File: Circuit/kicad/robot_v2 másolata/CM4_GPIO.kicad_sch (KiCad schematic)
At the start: 28 parts, among them J1 Conn_01x03, J2 Conn_02x07_Odd_Even, J3 Conn_01x03, J7 Micro_SD_Card_Det, J8 THD-20-R, J9 THD-02-R, U1 TPD4EUSB30, U18 RT9742GGJ5, U2 TPD4EUSB30, U3 MagJack-A70-112-331N126, U5 74LVC1G07SE-7, U9 74LVC1G07SE-7

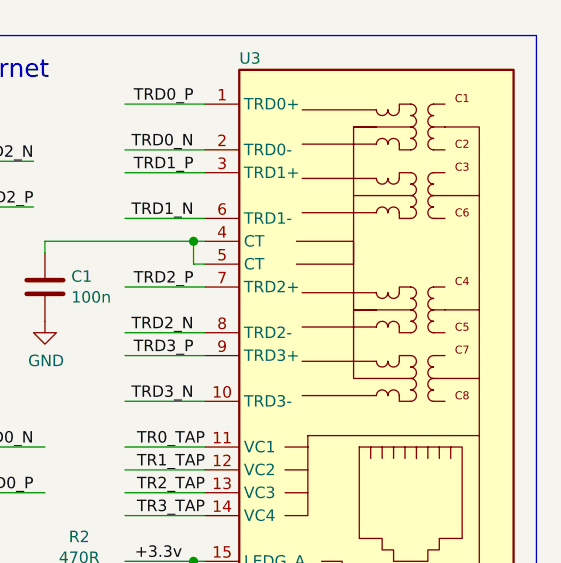
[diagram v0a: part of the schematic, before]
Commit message: kicad i2c schematic updated: gyto i2c bugfixes, +add new datasheets
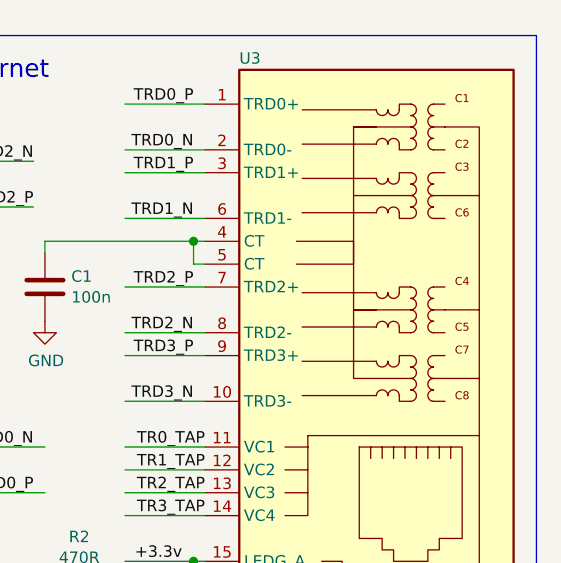
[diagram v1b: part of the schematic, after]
